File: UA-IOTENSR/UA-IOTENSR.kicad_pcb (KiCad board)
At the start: 4 copper layers, 31 parts, among them IC1 BQ2000TPN-B5, J1 Conn_01x04_Male, J2 ZX62-AB-5PA_31_, SW1 SW_DPST, U1 ESP32-S3-MINI-1, U2 AP63203WU

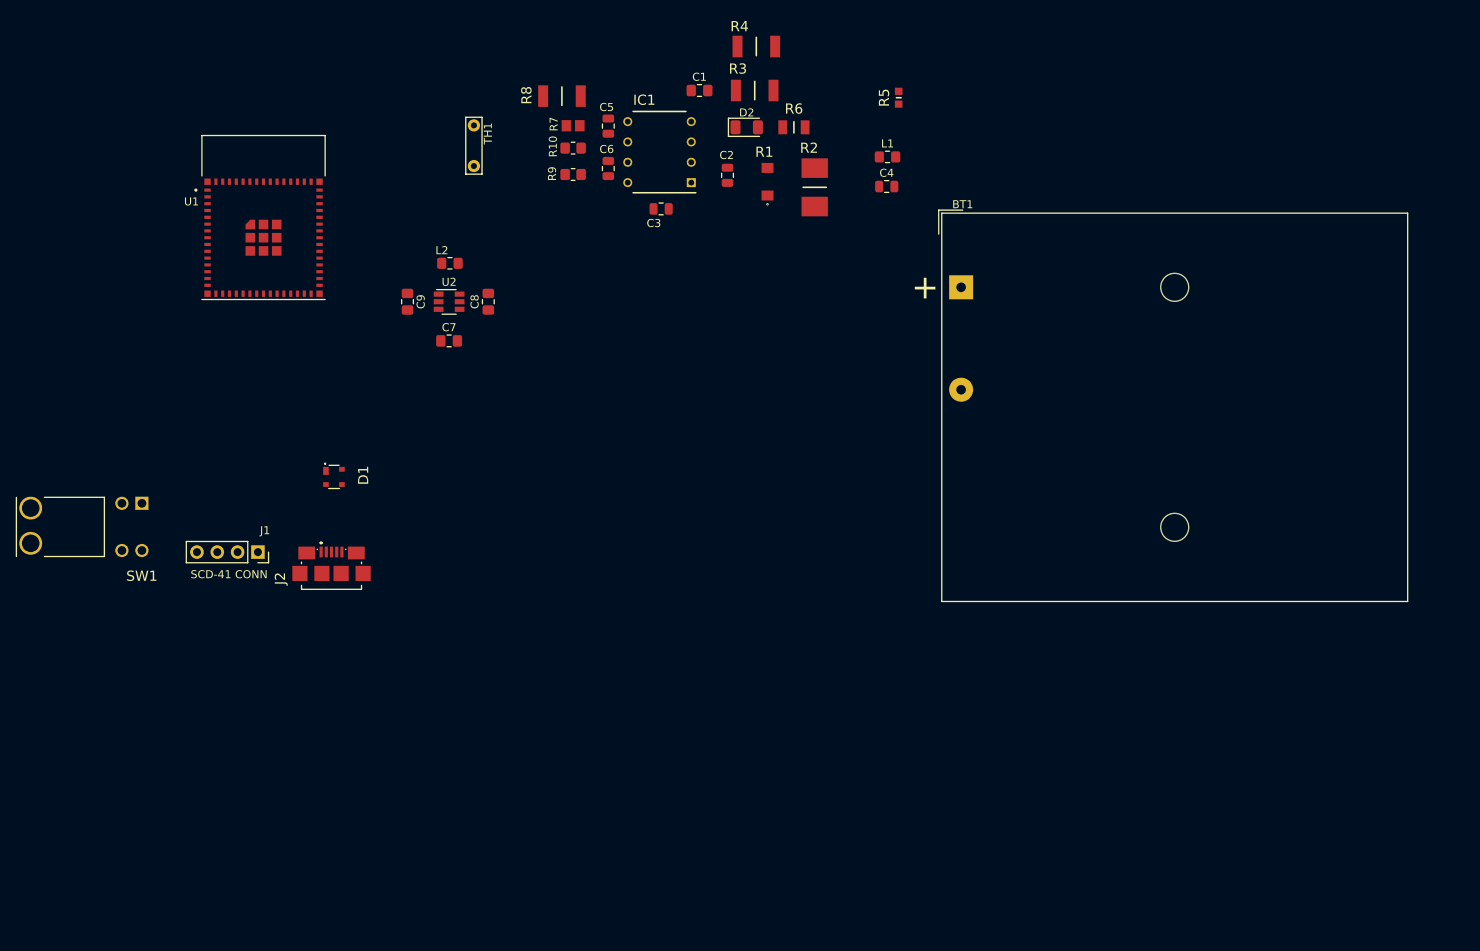
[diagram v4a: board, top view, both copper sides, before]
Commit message: Updated resistor values within the schematic
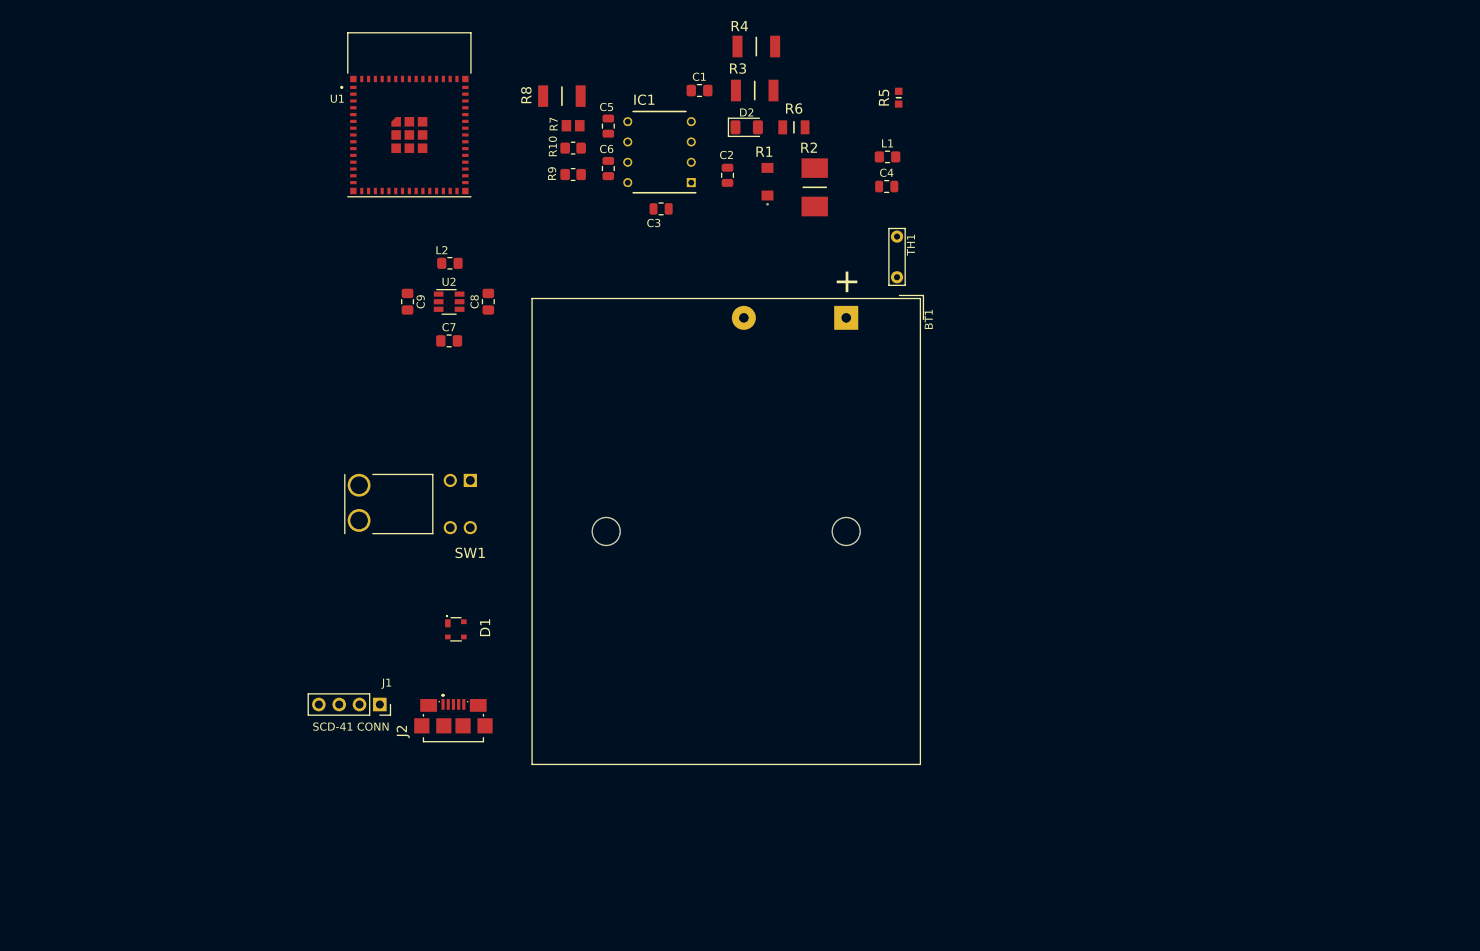
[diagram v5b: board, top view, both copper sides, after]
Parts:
- moved TH1 54.7 mm to (186.7, 50.8)
- moved SW1 41.1 mm to (133.3, 78.7)
- moved J1 24.4 mm to (122.0, 106.8)
- moved J2 24.4 mm to (131.2, 108.8)
- moved D1 24.4 mm to (131.5, 97.3)
- moved U1 22.3 mm to (125.7, 35.6)
- moved BT1 14.9 mm to (180.3, 58.4), turned to 270 degrees

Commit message: Placed james on silkscreen :sunglasses:
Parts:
- added G***: LOGO, SamacSys_Parts:negative_cropped_james, F.Cu at (112.1, 60.6)

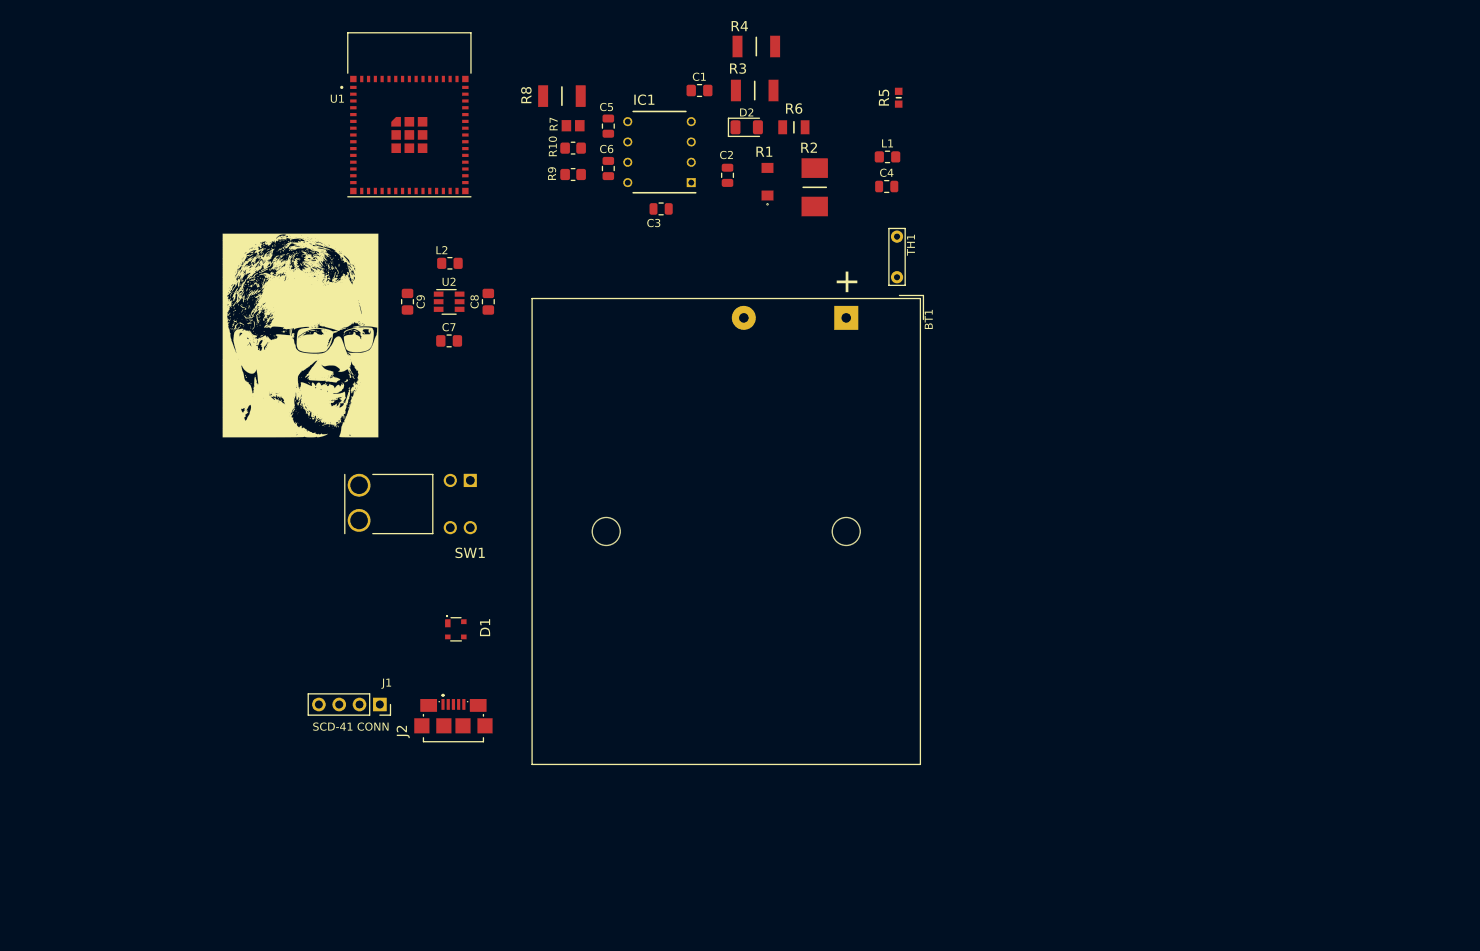
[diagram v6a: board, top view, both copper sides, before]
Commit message: removed dc+-, ground pour, M3 mounting holes
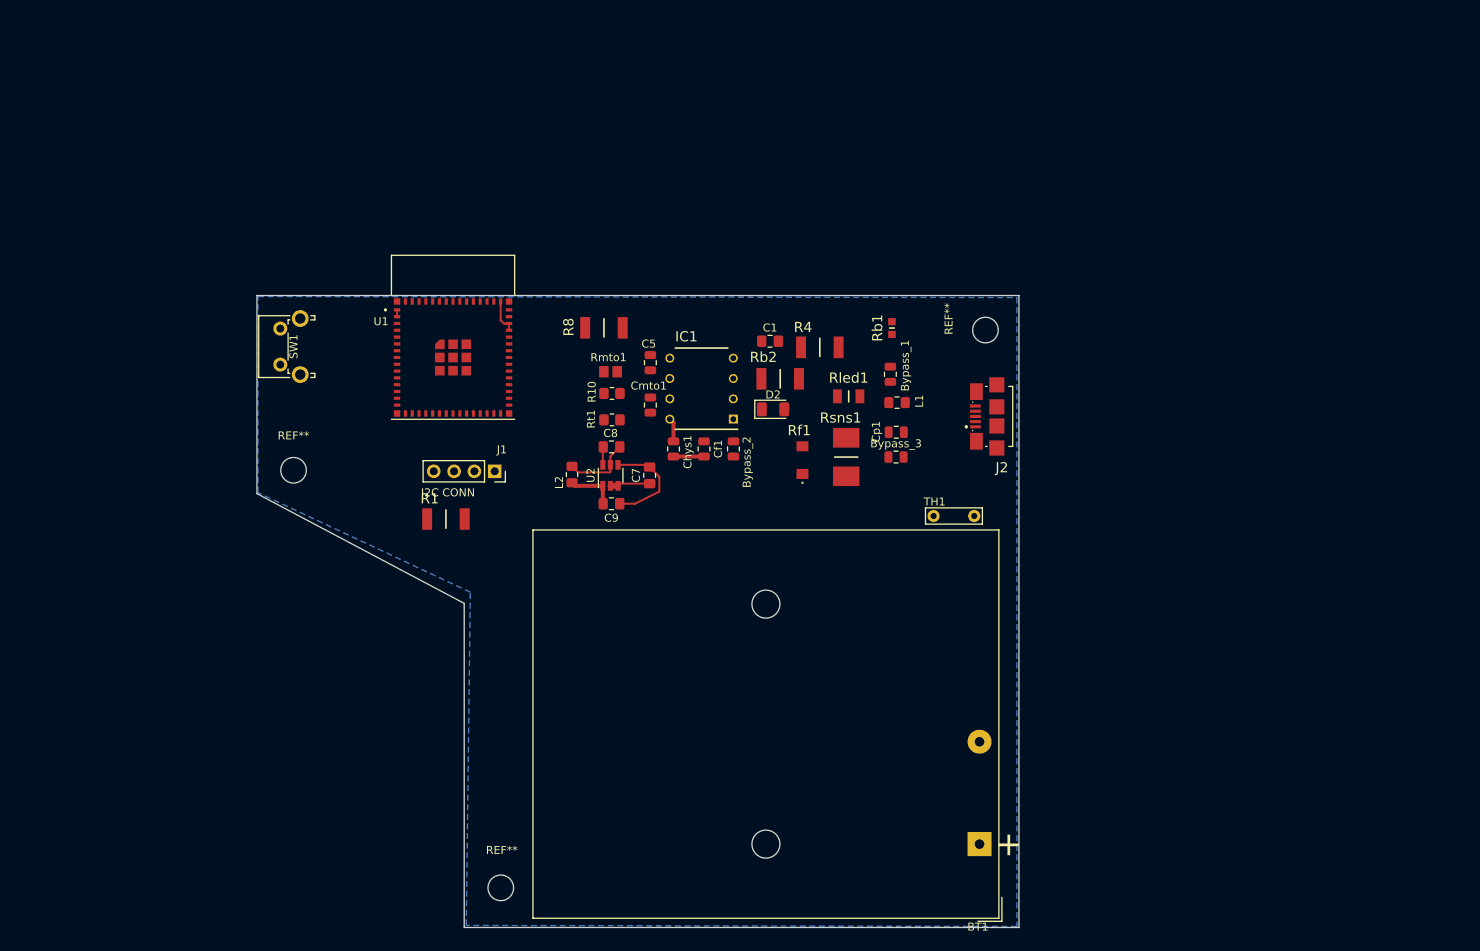
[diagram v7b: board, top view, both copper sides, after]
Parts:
- removed D1: PRTR5V0U2X,215, SamacSys_Parts:PRTR5V0U2X
- removed G***: LOGO, SamacSys_Parts:negative_cropped_james
- added Bypass_1: 10u, Capacitor_SMD:C_0805_2012Metric, F.Cu at (185.9, 65.5)
- added Bypass_2: 0.1u, Capacitor_SMD:C_0805_2012Metric, F.Cu at (166.2, 74.8)
- added Bypass_3: 470u, Capacitor_SMD:C_0805_2012Metric, F.Cu at (186.6, 75.8)
- added R1: 10k, SamacSys_Parts:RESC5025X70N, F.Cu at (130.3, 83.6)
- added REF**: MountingHole_3.2mm_M3, MountingHole:MountingHole_3.2mm_M3, F.Cu at (111.3, 77.5)
- added REF**: MountingHole_3.2mm_M3, MountingHole:MountingHole_3.2mm_M3, F.Cu at (137.2, 129.7)
- added REF**: MountingHole_3.2mm_M3, MountingHole:MountingHole_3.2mm_M3, F.Cu at (197.7, 59.9)
- D2: value LED -> Status_LED
- L1: value 30u -> 50u
- Rmto1: renamed from R7; value 22.1k -> 56k
- Rsns1: renamed from R2; value 50m -> 0.1
- Rt1: renamed from R9; value 4.8047k -> 4.7k
- SW1: value SW_DPST -> SW_Push; footprint SamacSys_Parts:PB400EEQR1BLK -> Button_Switch_THT:SW_Tactile_SPST_Angled_PTS645Vx58-2LFS
- moved J2 77.3 mm to (198.5, 70.7), turned to 90 degrees
- moved BT1 67.9 mm to (197.0, 124.2), turned to 180 degrees
- moved R4 38.4 mm to (177.0, 62.1)
- moved Rb2 36.2 mm to (172.1, 66.0)
- moved C9 35.9 mm to (151.0, 81.7), turned to 0 degrees
- moved D2 35.4 mm to (171.2, 69.8)
- moved Rf1 35.1 mm to (174.9, 76.2)
- moved Cf1 34.3 mm to (162.6, 74.8)
- moved Rled1 34.3 mm to (180.6, 68.2)
- moved Rsns1 33.9 mm to (180.3, 75.8)
- moved TH1 33.2 mm to (193.8, 83.2), turned to 180 degrees
- moved C1 32.6 mm to (170.8, 61.3)
- moved J1 32.5 mm to (136.4, 77.6)
- moved Rmto1 31.1 mm to (150.9, 65.2)
- moved R10 31.1 mm to (151.1, 67.9)
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- renumbered C2 to Cf1, C3 to Chys1, C6 to Cmto1, C4 to Cp1, R5 to Rb1, R3 to Rb2, R1 to Rf1, R6 to Rled1
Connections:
- Cp1 pad 2: BAT- -> GNDREF
- J2 pad 2: D- -> Net-(J2-Pad2)
- J2 pad 3: D+ -> Net-(J2-Pad3)
- J2 pad 5: BAT- -> Net-(J2-Pad5)
- J2 pad MP1: BAT- -> Net-(J2-Pad5)
- J2 pad MP2: BAT- -> Net-(J2-Pad5)
- J2 pad MP3: BAT- -> Net-(J2-Pad5)
- J2 pad MP4: BAT- -> Net-(J2-Pad5)
- J2 pad MP5: BAT- -> Net-(J2-Pad5)
- J2 pad MP6: BAT- -> Net-(J2-Pad5)
- R8 pad 1: Net-(R10-Pad1) -> Net-(R8-Pad1)
- Rf1 pad 2: BAT- -> GNDREF
- Rsns1 pad 1: BAT- -> GNDREF
- Rt1 pad 1: DC+ -> Net-(R8-Pad1)
- Rt1 pad 2: Net-(R10-Pad1) -> BAT-
- SW1 pad 1: Net-(SW1-Pad1) -> PUSHBUTTON
- SW1 pad 2: BAT- -> Net-(R1-Pad1)
- TH1 pad 1: BAT- -> DC+
- TH1 pad 2: Net-(R10-Pad1) -> Net-(R8-Pad1)
- U1 pad 23: D- -> Net-(U1-Pad23)
- U1 pad 24: D+ -> Net-(U1-Pad24)
- U1 pad 44: Net-(SW1-Pad1) -> Net-(U1-Pad44)
- U1 pad 6: Net-(U1-Pad6) -> PUSHBUTTON
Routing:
- net BAT-: track 0.00 -> 18.2 mm
- net Net-(C8-Pad1): track 0.00 -> 8.73 mm
- net +3V3: track 0.00 -> 6.26 mm
- net BAT+: track 0.00 -> 5.01 mm
- net Net-(Cf1-Pad1): track 0.00 -> 3.81 mm
- net Net-(Chys1-Pad1): track 0.00 -> 2.97 mm
- net Net-(C8-Pad2): track 0.00 -> 2.39 mm
- added copper zone on B.Cu, net BAT-
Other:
- board outline added: 95.2 x 79 mm
- rule trace_min: 0.2 -> 0.02
- board text added: "I2C CONN"
- board text removed: "SCD-41 CONN"

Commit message: pushbutton, esp antenna, condensing, title + james!!
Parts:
- removed the REF** at (111.3, 77.5)
- removed the REF** at (137.2, 129.7)
- added G***: LOGO, SamacSys_Parts:negative_cropped_james, F.Cu at (149.4, 110.2)
- added REF**: MountingHole_3.2mm_M3, MountingHole:MountingHole_3.2mm_M3, F.Cu at (126.7, 61.0)
- added REF**: MountingHole_3.2mm_M3, MountingHole:MountingHole_3.2mm_M3, F.Cu at (126.9, 129.7)
- moved SW1 20.0 mm to (124.8, 77.2)
- moved U1 16.6 mm to (146.9, 68.6)
- moved R1 16.1 mm to (127.6, 67.7)
- moved Cf1 15.4 mm to (177.9, 74.4)
- moved J1 15.0 mm to (150.5, 82.7)
- moved Rb2 11.8 mm to (183.9, 66.7)
- moved D2 11.8 mm to (183.0, 70.2)
- moved C7 11.7 mm to (167.4, 77.7)
- moved C8 11.7 mm to (162.7, 74.2)
- moved C5 11.7 mm to (167.5, 63.6)
- moved C9 11.7 mm to (162.7, 81.3)
- moved Chys1 11.7 mm to (170.4, 74.4)
- moved Cmto1 11.7 mm to (167.5, 68.9)
- moved IC1 11.7 mm to (173.9, 66.9)
- moved L2 11.7 mm to (157.7, 77.6)
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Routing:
- net BAT-: track 18.2 -> 12.9 mm
- net Net-(Cf1-Pad1): track 3.81 -> 0.00 mm
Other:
- board size 95.2 x 79 mm -> 80 x 79.1 mm
- board text added: "ECE 490/491 Capstone Project Group 10 IOTENSR"
